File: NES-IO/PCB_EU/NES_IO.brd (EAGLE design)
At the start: 72.8 x 77.5 mm, 65 parts, among them IC1 74HC125D, J1.1 MY_JUMPER, J1.2 MY_JUMPER, J2.2 10k, J4.C MY_JUMPER, J4.V MY_JUMPER, J6 MY_JUMPER, J7 MY_JUMPER

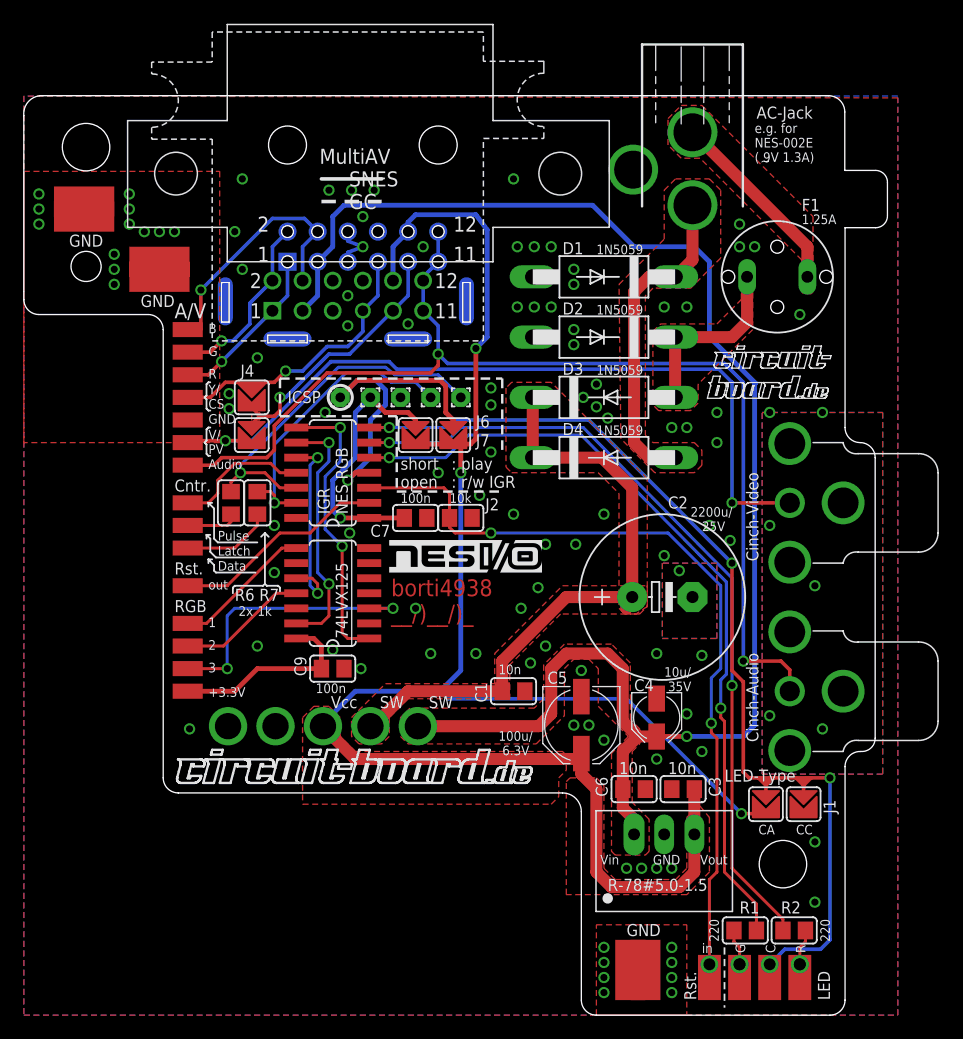
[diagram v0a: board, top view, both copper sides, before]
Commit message: Common design for MultiAV (from SNES or GC) and FR-NES-RGB jack
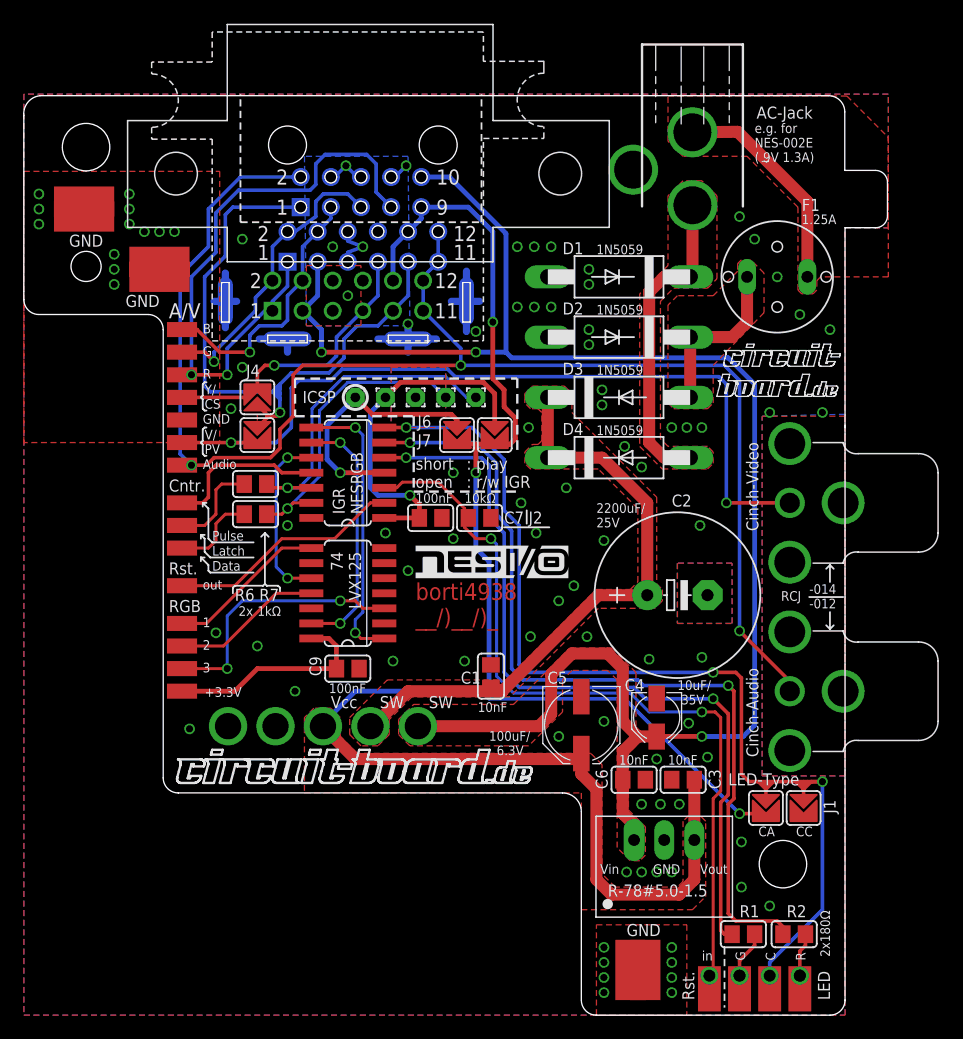
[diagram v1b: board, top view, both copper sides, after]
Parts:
- added U$8: NESFR_JACK2, nintendo:NESFR_JACK2
- moved J7 6.67 mm to (39.7, 48.9)
- moved R7 2.60 mm to (19.5, 44.8), turned to 180 degrees
- moved C1 2.29 mm to (39.4, 28.6), turned to 90 degrees
- moved U$3 2.27 mm to (33.0, 36.8)
- moved J2.2 1.59 mm to (38.4, 41.9)
- moved C2 1.28 mm to (55.1, 35.4)
- moved ICSP3 1.27 mm to (33.0, 52.1)
- moved ICSP4 1.27 mm to (35.6, 52.1)
- moved ICSP5 1.27 mm to (38.1, 52.1)
- moved C9 1.27 mm to (27.3, 29.2)
- moved IC1 1.27 mm to (27.3, 35.6)
- moved ICSP1 1.27 mm to (27.9, 52.1)
- moved ICSP2 1.27 mm to (30.5, 52.1)
- moved U$5 1.27 mm to (27.3, 45.7)
- moved C7 1.27 mm to (34.3, 41.9)
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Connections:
- net DC2: now also U$8.P$10
- net GND: now also U$8.P$4, U$8.P$6, U$8.P$8
- net N$30: now also J4.C.P$1, U$8.P$1; no longer J4.C.P$2
- net N$5: now also U$8.P$2
- net N$6: now also U$8.P$3
- net N$7: now also J4.C.P$2; no longer J4.C.P$1
- net N$8: now also U$8.P$5
- net N$9: now also U$8.P$7
- net VCC: now also U$8.P$9
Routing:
- net N$9: track 14.0 -> 51.4 mm, vias 1 -> 2
- net N$5: track 94.4 -> 126.9 mm, vias 2 -> 3
- net N$30: track 22.7 -> 54.3 mm
- net GND: track 6.21 -> 36.5 mm, vias 109 -> 92
- net DC2: track 132.0 -> 142.7 mm, vias 1 -> 3
- net N$8: track 15.3 -> 25.1 mm
- net N$32: track 29.2 -> 21.5 mm
- net N$31: track 22.4 -> 29.9 mm
- net VCC: track 150.7 -> 155.1 mm
- net N$14: track 67.9 -> 72.1 mm
- net N$20: track 4.42 -> 7.90 mm
- net N$34: track 30.8 -> 27.6 mm
- net N$29: track 67.1 -> 69.5 mm
- net AC1A: track 16.3 -> 18.5 mm
- net N$21: track 11.5 -> 13.7 mm
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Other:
- outline, holes or cut-outs redrawn
- board text added: "(Fr-RGB) NES"
- board text added: "-014 -012"
- board text added: "100nF"
- board text added: "100uF/ 6.3V"
- board text added: "10kΩ"
- board text added: "10nF"
- board text added: "10uF/ 35V"
- board text added: "1kΩ"
- board text added: "2200uF/ 25V"
- board text added: "2x180Ω"
- board text added: "74 LVX125"
- board text added: "IGR NESRGB"
- board text added: "PCB-Design: borti4938, srdwa, Sputnick"
- board text added: "RCJ"
- board text added: "Version: 20151220EU"
- board text removed: "100n"
- board text removed: "100u/ 6.3V"
- board text removed: "10k"
- board text removed: "10n"
- board text removed: "10u/ 35V"
- board text removed: "1k"
- board text removed: "220"
- board text removed: "2200u/ 25V"
- board text removed: "74LVX125"
- board text removed: "IGR NES RGB"
- board text removed: "MultiAV SNES GC"
- board text removed: "PCB-Design: srdwa, Sputnick, borti4938"
- board text removed: "Version: 20150321"
